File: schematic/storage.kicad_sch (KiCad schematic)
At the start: 7 parts, among them U2 27C256, U3 SCM2114AL, U4 SCM2114AL

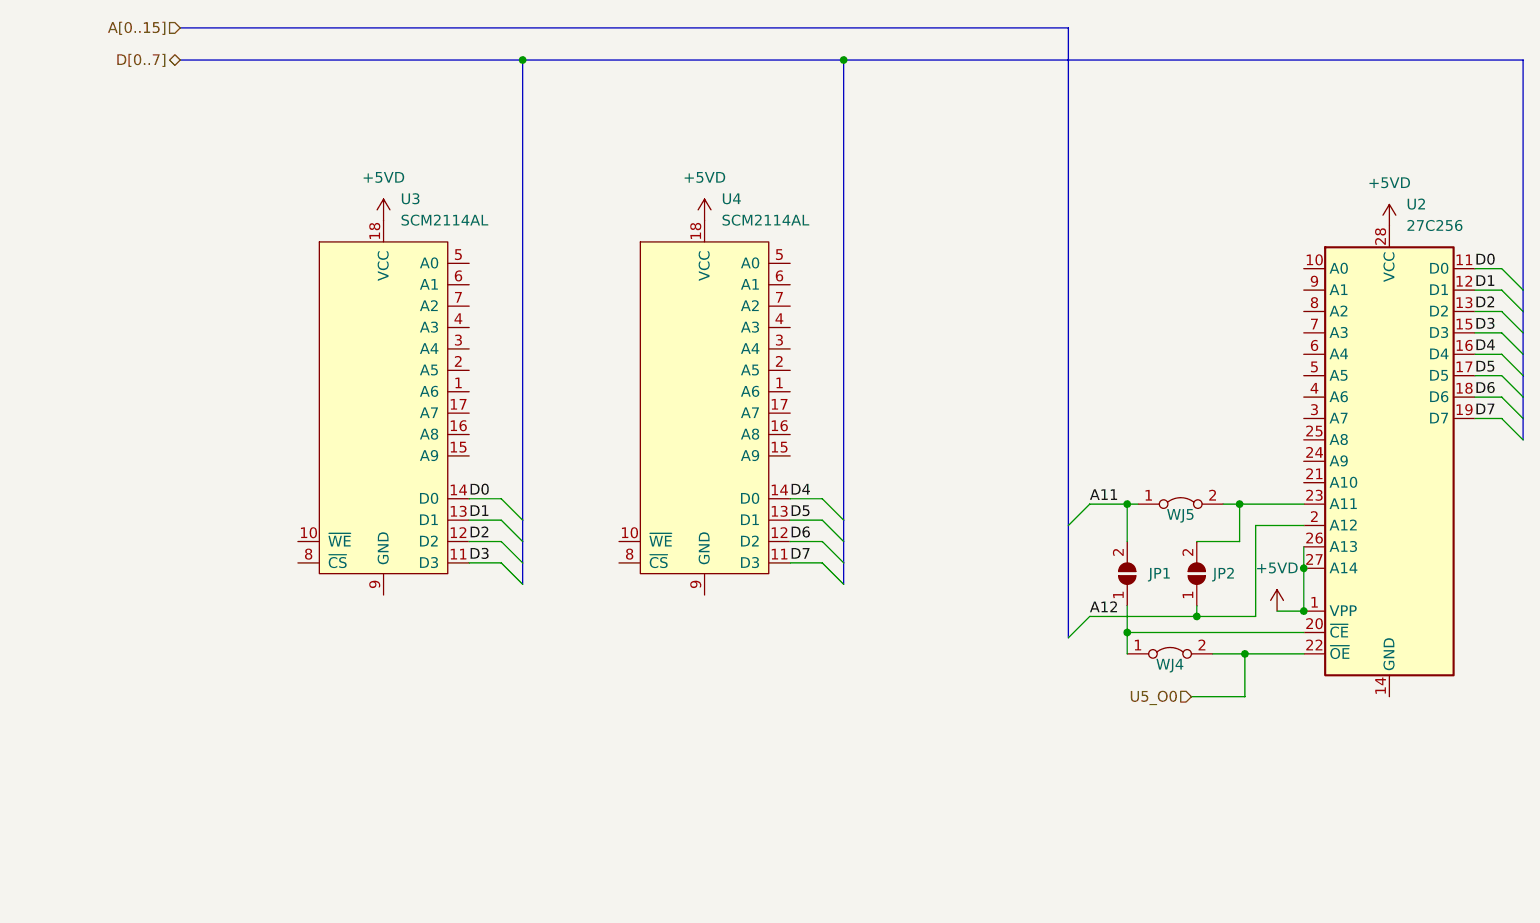
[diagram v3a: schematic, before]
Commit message: Up to pin 29 on z80 done. Address 0 to 10 left. Only tracing to its end point for the most part. Each chip gets traced chip to chip in this manned
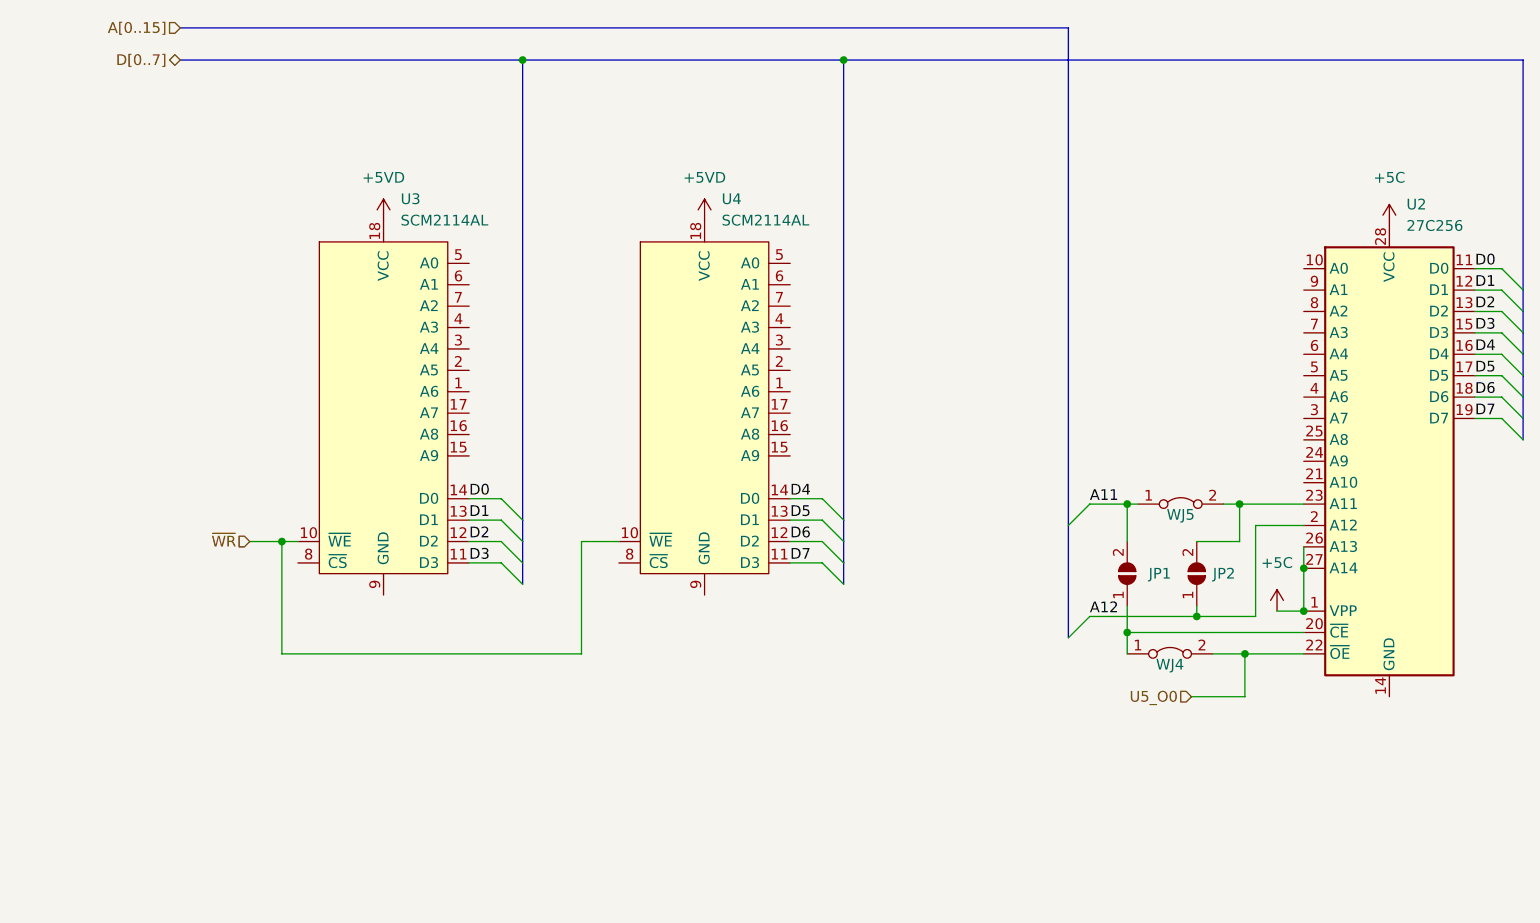
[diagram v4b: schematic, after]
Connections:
- net +5VD: no longer U2.1 (VPP), U2.26 (A13), U2.27 (A14), U2.28 (VCC)
- net ~{WR}: now reaches U3.10 (~{WE})
- net ~{WR}: now also U4.10 (~{WE})
- new net +5C: U2.1 (VPP), U2.26 (A13), U2.27 (A14), U2.28 (VCC)
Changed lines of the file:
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@@
   (junction (at 213.995 92.075) (diameter 0) (color 0 0 0 0)
   )
+  (junction (at 92.71 88.9) (diameter 0) (color 0 0 0 0)
+  )
   (junction (at 193.04 99.695) (diameter 0) (color 0 0 0 0)
   )
@@
     (stroke (width 0) (type default) (color 0 0 0 0))
   )
+  (wire (pts (xy 92.71 88.9) (xy 94.615 88.9))
+    (stroke (width 0) (type default) (color 0 0 0 0))
+  )
+  (wire (pts (xy 88.9 88.9) (xy 92.71 88.9))
+    (stroke (width 0) (type default) (color 0 0 0 0))
+  )
   (wire (pts (xy 153.035 86.36) (xy 156.845 86.36))
     (stroke (width 0) (type default) (color 0 0 0 0))
@@
     (stroke (width 0) (type default) (color 0 0 0 0))
   )
+  (wire (pts (xy 92.71 88.9) (xy 92.71 102.235))
+    (stroke (width 0) (type default) (color 0 0 0 0))
+  )
+  (wire (pts (xy 128.27 88.9) (xy 132.715 88.9))
+    (stroke (width 0) (type default) (color 0 0 0 0))
+  )
   (wire (pts (xy 114.935 88.9) (xy 118.745 88.9))
     (stroke (width 0) (type default) (color 0 0 0 0))
@@
     (stroke (width 0) (type default) (color 0 0 0 0))
   )
+  (wire (pts (xy 128.27 102.235) (xy 128.27 88.9))
+    (stroke (width 0) (type default) (color 0 0 0 0))
+  )
   (wire (pts (xy 234.315 71.755) (xy 237.49 71.755))
     (stroke (width 0) (type default) (color 0 0 0 0))
@@
     (stroke (width 0) (type default) (color 0 0 0 0))
   )
+  (wire (pts (xy 92.71 102.235) (xy 128.27 102.235))
+    (stroke (width 0) (type default) (color 0 0 0 0))
+  )
   (wire (pts (xy 204.47 84.455) (xy 206.375 84.455))
     (stroke (width 0) (type default) (color 0 0 0 0))
@@
   )
   (hierarchical_label "U5_O0" (shape input) (at 200.66 107.315 180)
+    (effects (font (size 1.27 1.27)) (justify right))
+  )
+  (hierarchical_label "~{WR}" (shape input) (at 88.9 88.9 180)
     (effects (font (size 1.27 1.27)) (justify right))
   )
@@
     (pin "9")
   )
-  (symbol (lib_id "power:+5VD") (at 210.82 97.155 0) (unit 1)
-    (in_bom yes) (on_board yes) (fields_autoplaced)
-    (property "Reference" "#PWR?" (id 0) (at 210.82 100.965 0)
-      (effects (font (size 1.27 1.27)) hide)
-    )
-    (property "Value" "+5VD" (id 1) (at 210.82 92.075 0))
-    (property "Footprint" "" (id 2) (at 210.82 97.155 0)
-      (effects (font (size 1.27 1.27)) hide)
-    )
-    (property "Datasheet" "" (id 3) (at 210.82 97.155 0)
+  (symbol (lib_id "power:+5C") (at 224.155 51.435 0) (unit 1)
+    (in_bom yes) (on_board yes) (fields_autoplaced)
+    (property "Reference" "#PWR?" (id 0) (at 224.155 55.245 0)
+      (effects (font (size 1.27 1.27)) hide)
+    )
+    (property "Value" "+5C" (id 1) (at 224.155 45.72 0))
+    (property "Footprint" "" (id 2) (at 224.155 51.435 0)
+      (effects (font (size 1.27 1.27)) hide)
+    )
+    (property "Datasheet" "" (id 3) (at 224.155 51.435 0)
       (effects (font (size 1.27 1.27)) hide)
     )
@@
     (pin "1")
     (pin "2")
+  )
+  (symbol (lib_id "power:+5C") (at 210.82 97.155 0) (unit 1)
+    (in_bom yes) (on_board yes) (fields_autoplaced)
+    (property "Reference" "#PWR?" (id 0) (at 210.82 100.965 0)
+      (effects (font (size 1.27 1.27)) hide)
+    )
+    (property "Value" "+5C" (id 1) (at 210.82 91.44 0))
+    (property "Footprint" "" (id 2) (at 210.82 97.155 0)
+      (effects (font (size 1.27 1.27)) hide)
+    )
+    (property "Datasheet" "" (id 3) (at 210.82 97.155 0)
+      (effects (font (size 1.27 1.27)) hide)
+    )
+    (pin "1")
   )
   (symbol (lib_id "power:+5VD") (at 142.875 50.8 0) (unit 1)
@@
     (pin "2")
   )
-  (symbol (lib_id "power:+5VD") (at 224.155 51.435 0) (unit 1)
-    (in_bom yes) (on_board yes) (fields_autoplaced)
-    (property "Reference" "#PWR?" (id 0) (at 224.155 55.245 0)
-      (effects (font (size 1.27 1.27)) hide)
-    )
-    (property "Value" "+5VD" (id 1) (at 224.155 46.355 0))
-    (property "Footprint" "" (id 2) (at 224.155 51.435 0)
-      (effects (font (size 1.27 1.27)) hide)
-    )
-    (property "Datasheet" "" (id 3) (at 224.155 51.435 0)
-      (effects (font (size 1.27 1.27)) hide)
-    )
-    (pin "1")
-  )
 )

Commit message: completed Z80 trace of PCB. off to a good start.
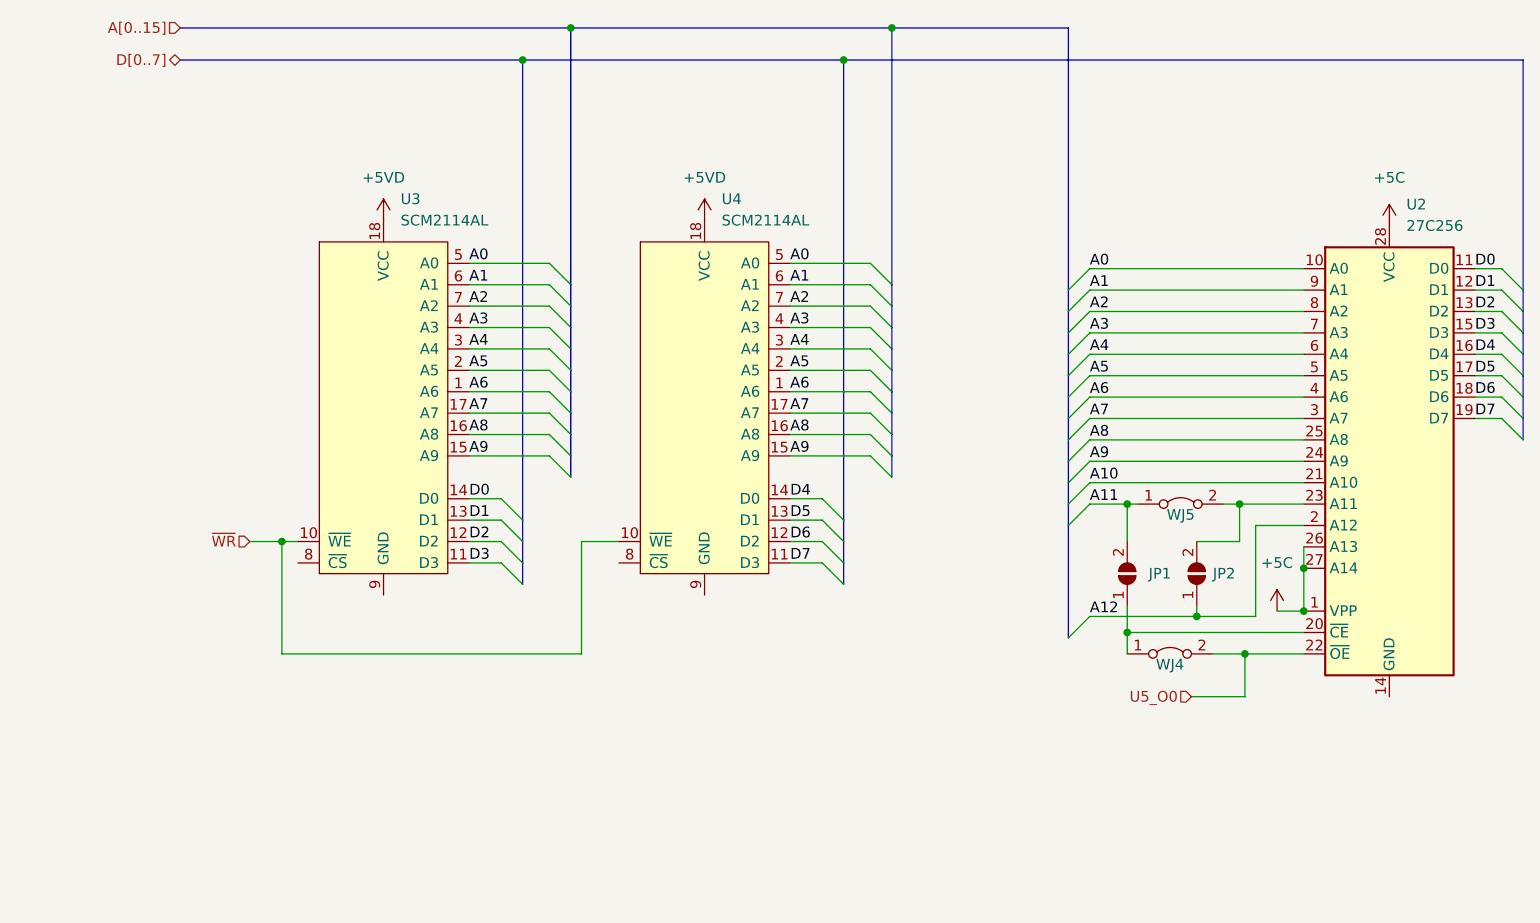
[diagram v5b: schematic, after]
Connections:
- net A6: now reaches U3.1 (A6)
- net A6: now also U2.4 (A6), U4.1 (A6)
- net A9: now reaches U3.15 (A9)
- net A9: now also U2.24 (A9), U4.15 (A9)
- net A8: now reaches U3.16 (A8)
- net A8: now also U2.25 (A8), U4.16 (A8)
- net A7: now reaches U3.17 (A7)
- net A7: now also U2.3 (A7), U4.17 (A7)
- net A5: now reaches U3.2 (A5)
- net A5: now also U2.5 (A5), U4.2 (A5)
- net A4: now reaches U3.3 (A4)
- net A4: now also U2.6 (A4), U4.3 (A4)
- net A3: now reaches U3.4 (A3)
- net A3: now also U2.7 (A3), U4.4 (A3)
- net A0: now reaches U3.5 (A0)
- net A0: now also U2.10 (A0), U4.5 (A0)
- net A1: now reaches U3.6 (A1)
- net A1: now also U2.9 (A1), U4.6 (A1)
- net A2: now reaches U3.7 (A2)
- net A2: now also U2.8 (A2), U4.7 (A2)
- net A10: now reaches U2.21 (A10)

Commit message: added rf modulation schematic, added dram to vdp. Fixed +5vc to +5v
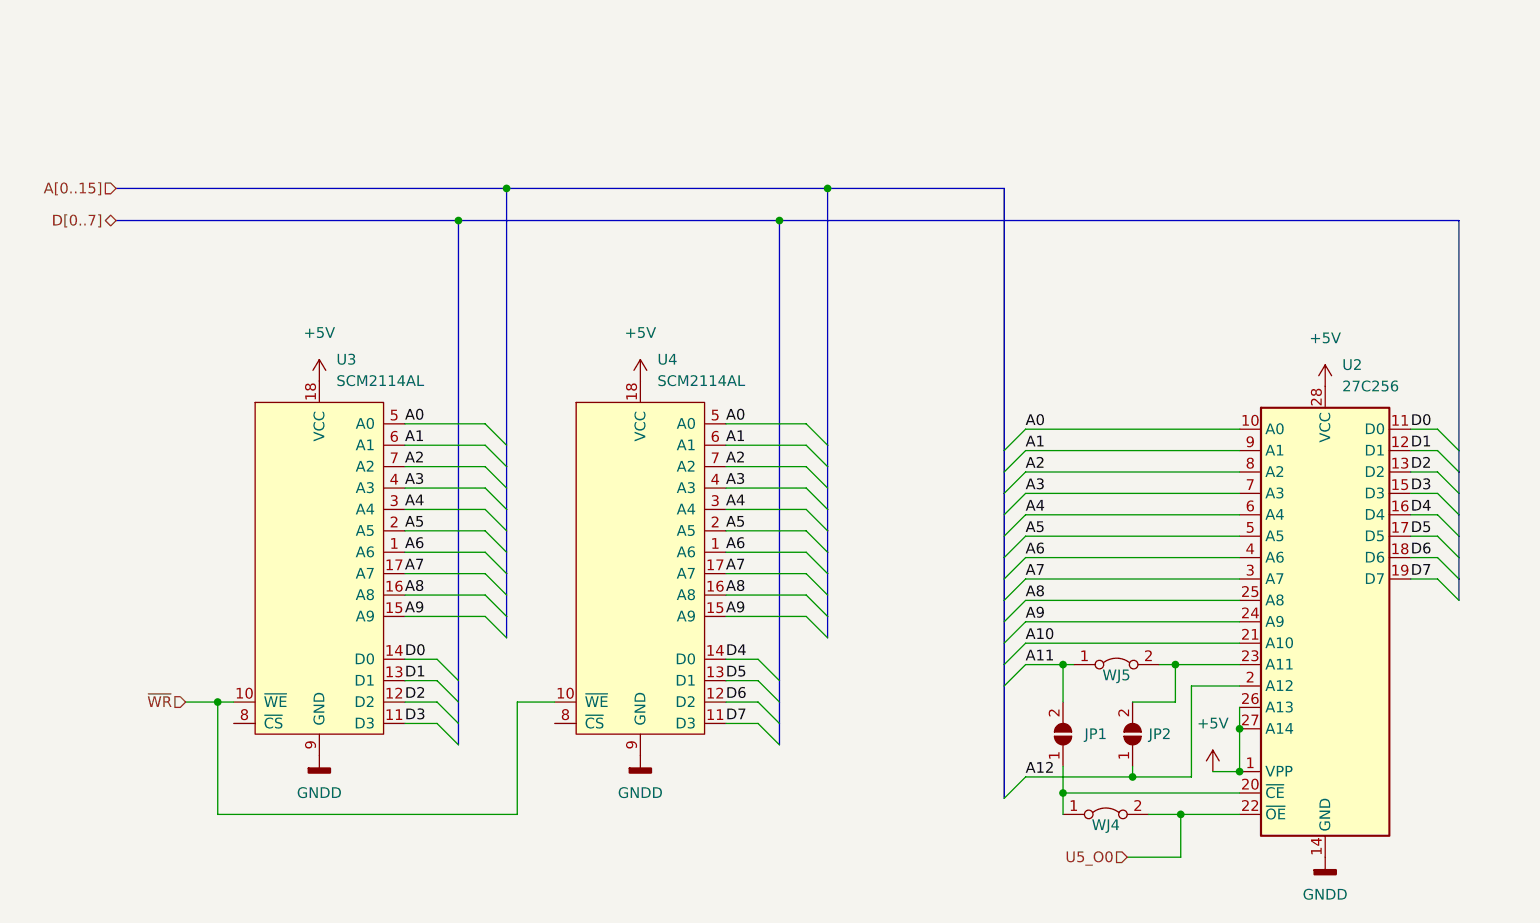
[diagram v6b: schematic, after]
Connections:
- net +5VD is gone; now on net +5V: U3.18 (VCC), U4.18 (VCC)
- net GNDD: now reaches U3.9 (GND)
- net GNDD: now also U2.14 (GND), U4.9 (GND)
- net +5C renamed +5V
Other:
- moved on the sheet: JP1, JP2, U2, U3, U4, WJ4, WJ5

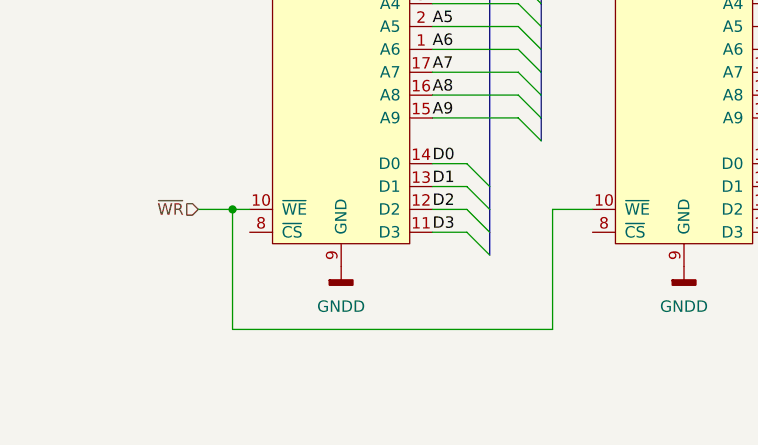
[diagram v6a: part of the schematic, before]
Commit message: added u5 decoder lines, need to rename for chip selects that they actually are in future.
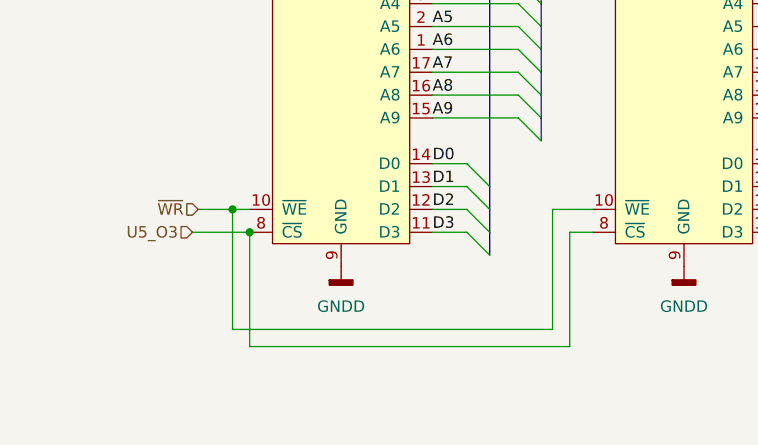
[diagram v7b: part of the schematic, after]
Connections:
- net U5_O3: now reaches U3.8 (~{CS})
- net U5_O3: now also U4.8 (~{CS})
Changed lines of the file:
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@@
   (junction (at 185.42 118.745) (diameter 0) (color 0 0 0 0)
   )
+  (junction (at 86.995 110.49) (diameter 0) (color 0 0 0 0)
+  )
   (bus_entry (at 178.435 88.265) (size 2.54 -2.54)
     (stroke (width 0) (type default) (color 0 0 0 0))
@@
     (stroke (width 0) (type default) (color 0 0 0 0))
   )
+  (wire (pts (xy 80.645 110.49) (xy 86.995 110.49))
+    (stroke (width 0) (type default) (color 0 0 0 0))
+  )
   (wire (pts (xy 107.315 80.01) (xy 116.84 80.01))
     (stroke (width 0) (type default) (color 0 0 0 0))
@@
     (stroke (width 0) (type default) (color 0 0 0 0))
   )
+  (wire (pts (xy 122.555 110.49) (xy 125.095 110.49))
+    (stroke (width 0) (type default) (color 0 0 0 0))
+  )
   (bus (pts (xy 178.435 100.965) (xy 178.435 103.505))
     (stroke (width 0) (type default) (color 0 0 0 0))
@@
     (stroke (width 0) (type default) (color 0 0 0 0))
   )
+  (wire (pts (xy 122.555 123.19) (xy 122.555 110.49))
+    (stroke (width 0) (type default) (color 0 0 0 0))
+  )
   (bus (pts (xy 119.38 92.71) (xy 119.38 95.25))
     (stroke (width 0) (type default) (color 0 0 0 0))
@@
     (stroke (width 0) (type default) (color 0 0 0 0))
   )
+  (wire (pts (xy 86.995 110.49) (xy 86.995 123.19))
+    (stroke (width 0) (type default) (color 0 0 0 0))
+  )
   (bus (pts (xy 157.48 46.99) (xy 157.48 77.47))
     (stroke (width 0) (type default) (color 0 0 0 0))
@@
   )
   (wire (pts (xy 200.66 106.045) (xy 206.375 106.045))
+    (stroke (width 0) (type default) (color 0 0 0 0))
+  )
+  (wire (pts (xy 86.995 123.19) (xy 122.555 123.19))
     (stroke (width 0) (type default) (color 0 0 0 0))
   )
@@
     (effects (font (size 1.27 1.27)) (justify right))
   )
+  (hierarchical_label "U5_O3" (shape input) (at 80.645 110.49 180)
+    (effects (font (size 1.27 1.27)) (justify right))
+  )
